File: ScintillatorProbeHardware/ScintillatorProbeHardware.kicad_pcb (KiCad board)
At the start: 2 copper layers, 99 x 80.5 mm, 14 parts

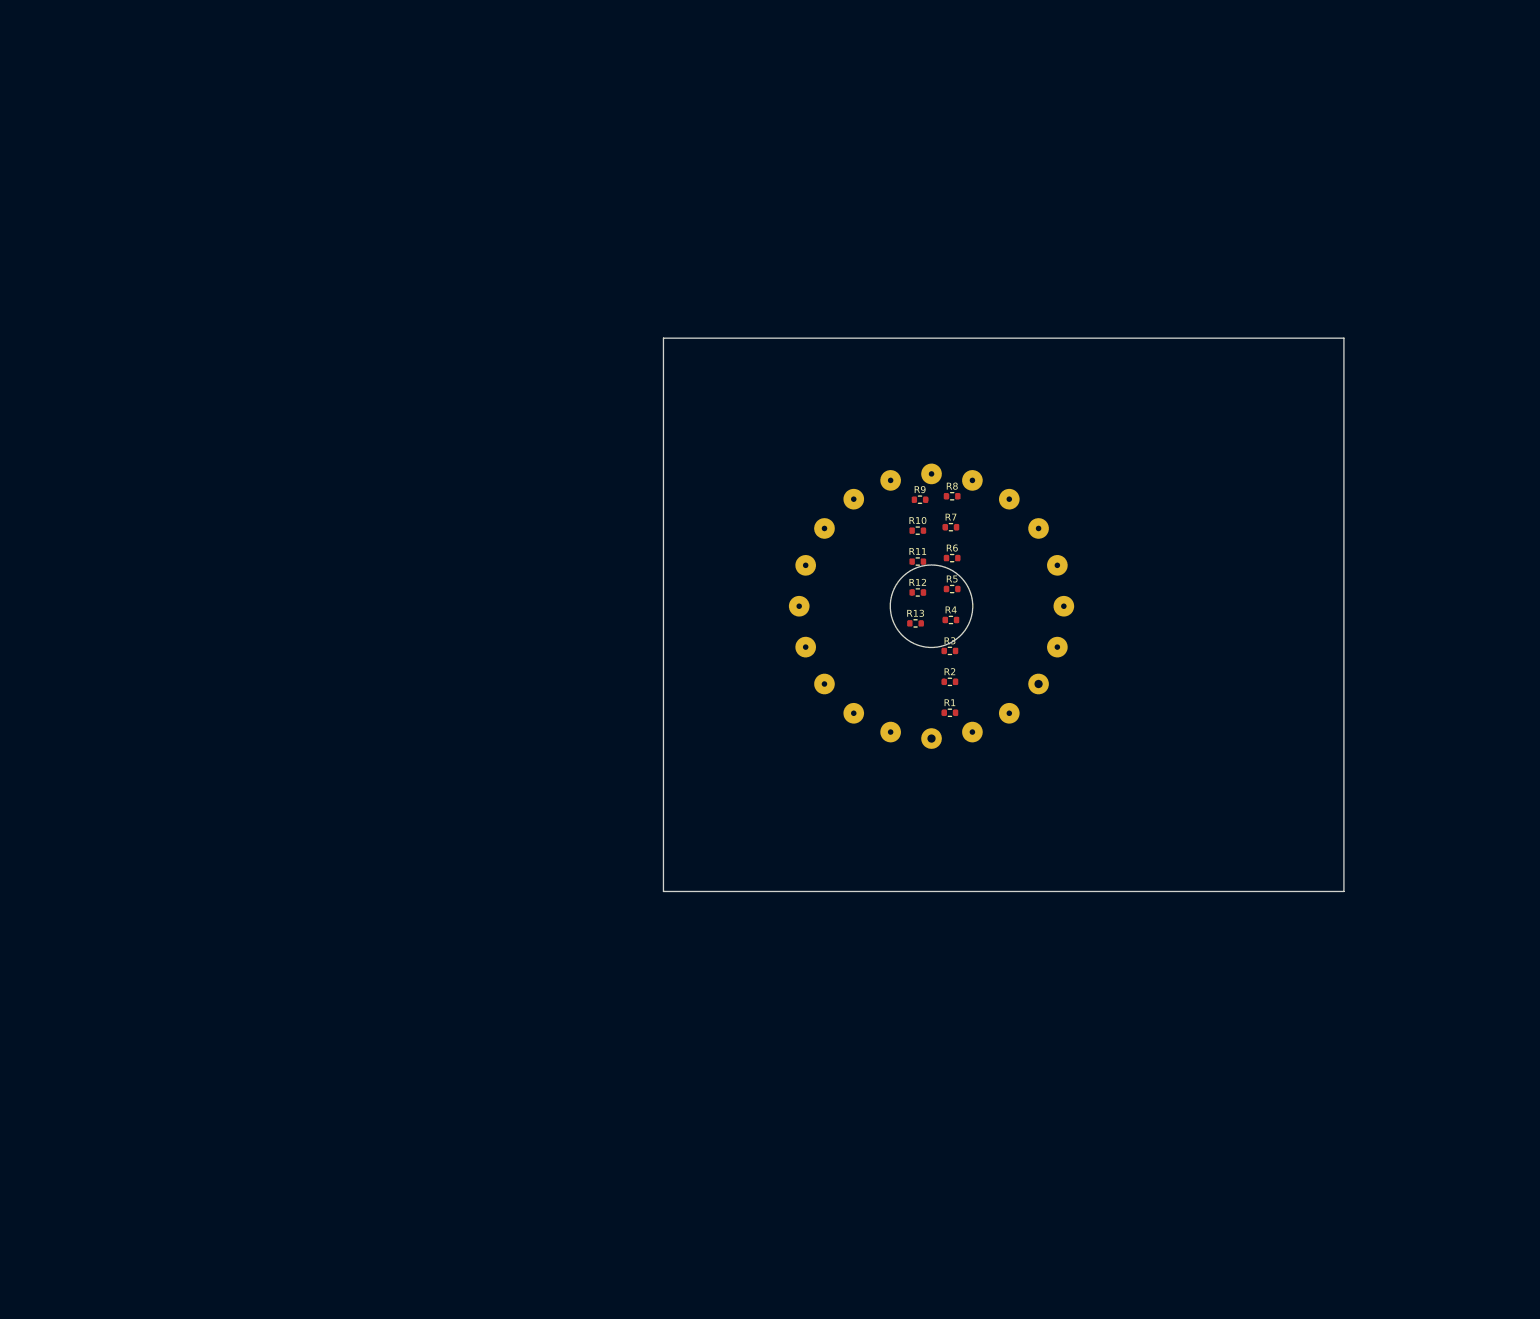
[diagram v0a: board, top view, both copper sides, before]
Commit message: PCB layout started, firmware modified for new peak detector
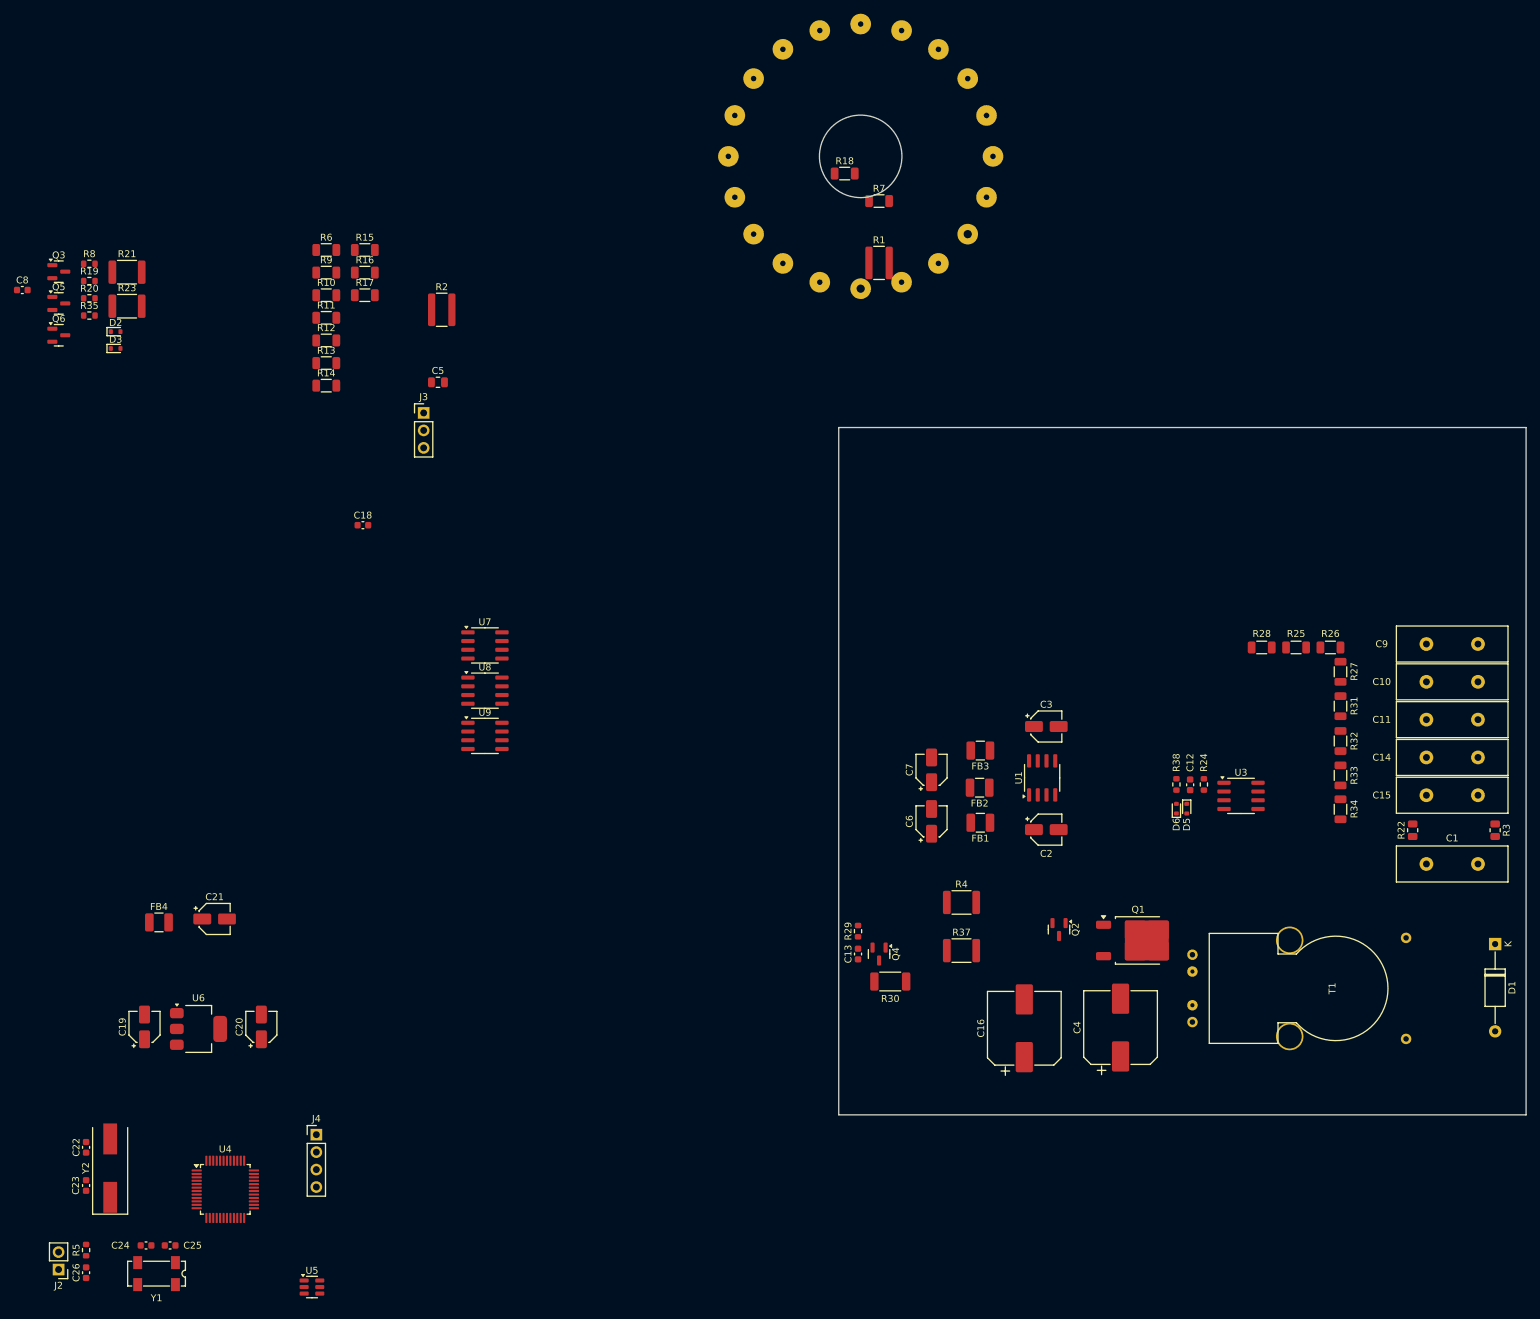
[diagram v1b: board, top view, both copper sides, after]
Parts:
- removed the R7 at (158.3, 70.5)
- added C1: 10n/3000V, Capacitor_THT:C_Disc_D16.0mm_W5.0mm_P7.50mm, F.Cu at (227.5, 119.5)
- added C10: 10n, Capacitor_THT:C_Disc_D16.0mm_W5.0mm_P7.50mm, F.Cu at (227.5, 93.0)
- added C11: 10n, Capacitor_THT:C_Disc_D16.0mm_W5.0mm_P7.50mm, F.Cu at (227.5, 98.5)
- added C12: 100n, Capacitor_SMD:C_0603_1608Metric, F.Cu at (193.1, 108.0)
- added C13: 1u, Capacitor_SMD:C_0603_1608Metric, F.Cu at (144.8, 132.6)
- added C14: 10n, Capacitor_THT:C_Disc_D16.0mm_W5.0mm_P7.50mm, F.Cu at (227.5, 104.0)
- added C15: 10n, Capacitor_THT:C_Disc_D16.0mm_W5.0mm_P7.50mm, F.Cu at (227.5, 109.5)
- added C16: 1000u, Capacitor_SMD:CP_Elec_10x10.5, F.Cu at (169.0, 143.4)
- added C18: 100n, Capacitor_SMD:C_0603_1608Metric, F.Cu at (72.8, 70.2)
- added C19: 10u, Capacitor_SMD:CP_Elec_4x5.4, F.Cu at (41.0, 143.2)
- added C2: 10u, Capacitor_SMD:CP_Elec_4x5.4, F.Cu at (172.2, 114.5)
- added C20: 10u, Capacitor_SMD:CP_Elec_4x5.4, F.Cu at (58.0, 143.2)
- added C21: 10u, Capacitor_SMD:CP_Elec_4x5.4, F.Cu at (51.2, 127.5)
- added C22: 20p, Capacitor_SMD:C_0603_1608Metric, F.Cu at (32.5, 160.7)
- added C23: 20p, Capacitor_SMD:C_0603_1608Metric, F.Cu at (32.5, 166.3)
- added C24: 20p, Capacitor_SMD:C_0603_1608Metric, F.Cu at (41.2, 175.0)
- added C25: 20p, Capacitor_SMD:C_0603_1608Metric, F.Cu at (44.7, 175.0)
- added C26: 100n, Capacitor_SMD:C_0603_1608Metric, F.Cu at (32.5, 179.0)
- added C3: 10u, Capacitor_SMD:CP_Elec_4x5.4, F.Cu at (172.2, 99.5)
- added C4: 1000u, Capacitor_SMD:CP_Elec_10x10.5, F.Cu at (183.0, 143.3)
- added C5: 10u, Capacitor_SMD:C_0805_2012Metric, F.Cu at (83.7, 49.4)
- added C6: 10u, Capacitor_SMD:CP_Elec_4x5.4, F.Cu at (155.5, 113.3)
- added C7: 10u, Capacitor_SMD:CP_Elec_4x5.4, F.Cu at (155.5, 105.8)
- added C8: 10n, Capacitor_SMD:C_0603_1608Metric, F.Cu at (23.2, 36.0)
- added C9: 10n, Capacitor_THT:C_Disc_D16.0mm_W5.0mm_P7.50mm, F.Cu at (227.5, 87.5)
- added D1: 2CL71A, Diode_THT:D_A-405_P12.70mm_Horizontal, F.Cu at (237.5, 131.2)
- added D2: D_Schottky, Diode_SMD:D_SOD-523, F.Cu at (36.8, 42.0)
- added D3: D_Schottky, Diode_SMD:D_SOD-523, F.Cu at (36.8, 44.5)
- added D5: D_Schottky, Diode_SMD:D_SOD-523, F.Cu at (192.6, 111.5)
- added D6: D_Schottky, Diode_SMD:D_SOD-523, F.Cu at (191.1, 111.5)
- added FB1: 620Ω@1MHz, Inductor_SMD:L_1210_3225Metric, F.Cu at (162.6, 113.5)
- added FB2: 620Ω@1MHz, Inductor_SMD:L_1210_3225Metric, F.Cu at (162.5, 108.4)
- added FB3: 620Ω@1MHz, Inductor_SMD:L_1210_3225Metric, F.Cu at (162.6, 103.0)
- added FB4: 620Ω@1MHz, Inductor_SMD:L_1210_3225Metric, F.Cu at (43.1, 128.0)
- added J2: Conn_01x02, Connector_PinHeader_2.54mm:PinHeader_1x02_P2.54mm_Vertical, F.Cu at (28.5, 178.5)
- added J3: Conn_01x03, Connector_PinHeader_2.54mm:PinHeader_1x03_P2.54mm_Vertical, F.Cu at (81.6, 53.9)
- added J4: Conn_01x04, Connector_PinHeader_2.54mm:PinHeader_1x04_P2.54mm_Vertical, F.Cu at (66.0, 158.9)
- added Q1: 15N10, Package_TO_SOT_SMD:TO-252-2, F.Cu at (185.6, 130.6)
- added Q2: S8050, Package_TO_SOT_SMD:SOT-23, F.Cu at (174.1, 129.0)
- added Q3: S8050, Package_TO_SOT_SMD:SOT-23, F.Cu at (28.5, 33.3)
- added Q4: AO401, Package_TO_SOT_SMD:SOT-23, F.Cu at (147.9, 132.6)
- added Q5: S8050, Package_TO_SOT_SMD:SOT-23, F.Cu at (28.5, 38.0)
- added Q6: S8050, Package_TO_SOT_SMD:SOT-23, F.Cu at (28.5, 42.6)
- added R13: 240k, Resistor_SMD:R_1206_3216Metric, F.Cu at (67.4, 46.6)
- added R14: 240k, Resistor_SMD:R_1206_3216Metric, F.Cu at (67.4, 49.9)
- added R15: 240k, Resistor_SMD:R_1206_3216Metric, F.Cu at (73.1, 30.2)
- added R16: 240k, Resistor_SMD:R_1206_3216Metric, F.Cu at (73.1, 33.5)
- added R17: 240k, Resistor_SMD:R_1206_3216Metric, F.Cu at (73.1, 36.8)
- added R19: 1k, Resistor_SMD:R_0603_1608Metric, F.Cu at (33.0, 34.7)
- added R20: 10k, Resistor_SMD:R_0603_1608Metric, F.Cu at (33.0, 37.2)
- added R21: 330R, Resistor_SMD:R_1812_4532Metric, F.Cu at (38.5, 33.4)
- added R22: 47k, Resistor_SMD:R_0805_2012Metric, F.Cu at (225.5, 114.6)
- added R23: 330R, Resistor_SMD:R_1812_4532Metric, F.Cu at (38.5, 38.4)
- added R24: 9k1, Resistor_SMD:R_0603_1608Metric, F.Cu at (195.1, 107.9)
- added R25: 1M, Resistor_SMD:R_1206_3216Metric, F.Cu at (208.5, 88.0)
- added R26: 1M, Resistor_SMD:R_1206_3216Metric, F.Cu at (213.5, 88.0)
- added R27: 1M, Resistor_SMD:R_1206_3216Metric, F.Cu at (215.0, 91.5)
- added R28: 1M, Resistor_SMD:R_1206_3216Metric, F.Cu at (203.5, 88.0)
- added R29: 100k, Resistor_SMD:R_0603_1608Metric, F.Cu at (144.8, 129.3)
- added R3: 47k, Resistor_SMD:R_0805_2012Metric, F.Cu at (237.5, 114.6)
- added R30: 47R, Resistor_SMD:R_2010_5025Metric, F.Cu at (149.5, 136.6)
- added R31: 1M, Resistor_SMD:R_1206_3216Metric, F.Cu at (215.0, 96.5)
- added R32: 1M, Resistor_SMD:R_1206_3216Metric, F.Cu at (215.0, 101.6)
- added R33: 1M, Resistor_SMD:R_1206_3216Metric, F.Cu at (215.0, 106.6)
- added R34: 1M, Resistor_SMD:R_1206_3216Metric, F.Cu at (215.0, 111.5)
- added R35: 1k, Resistor_SMD:R_0603_1608Metric, F.Cu at (33.0, 39.7)
- added R37: 330R, Resistor_SMD:R_1812_4532Metric, F.Cu at (159.9, 132.1)
- added R38: 1k, Resistor_SMD:R_0603_1608Metric, F.Cu at (191.1, 107.9)
- added T1: 24:1800, CustomParts:15kV_Transformer, F.Cu at (214.3, 137.6)
- added U1: ICL7660, Package_SO:SOIC-8_3.9x4.9mm_P1.27mm, F.Cu at (171.6, 107.0)
- added U3: LM358, Package_SO:SOIC-8_3.9x4.9mm_P1.27mm, F.Cu at (200.5, 109.6)
- added U4: STM32F103C8Tx, Package_QFP:LQFP-48_7x7mm_P0.5mm, F.Cu at (52.8, 166.8)
- added U5: USBLC6-2SC6, Package_TO_SOT_SMD:SOT-23-6, F.Cu at (65.4, 181.1)
- added U6: AMS1117-3.3, Package_TO_SOT_SMD:SOT-223-3_TabPin2, F.Cu at (48.9, 143.5)
- added U7: LM318N, Package_SO:SOIC-8_3.9x4.9mm_P1.27mm, F.Cu at (90.5, 87.7)
- added U8: LM318N, Package_SO:SOIC-8_3.9x4.9mm_P1.27mm, F.Cu at (90.5, 94.3)
- added U9: LM318N, Package_SO:SOIC-8_3.9x4.9mm_P1.27mm, F.Cu at (90.5, 100.9)
- added Y1: 32.768kHz, Crystal:Crystal_SMD_SeikoEpson_MC306-4Pin_8.0x3.2mm, F.Cu at (42.8, 179.1)
- added Y2: 8MHz, Crystal:Crystal_SMD_HC49-SD, F.Cu at (36.0, 163.8)
- R1: value 520K -> 620k; footprint Resistor_SMD:R_0603_1608Metric -> Resistor_SMD:R_1218_3246Metric
- R10, R11, R12, R6, R9: value 100K -> 240k; footprint Resistor_SMD:R_0603_1608Metric -> Resistor_SMD:R_1206_3216Metric
- R18: renamed from R13; value 100K -> 240k; footprint Resistor_SMD:R_0603_1608Metric -> Resistor_SMD:R_1206_3216Metric
- R2: value 100K -> 620k; footprint Resistor_SMD:R_0603_1608Metric -> Resistor_SMD:R_1218_3246Metric
- R4: value 100K -> 330R; footprint Resistor_SMD:R_0603_1608Metric -> Resistor_SMD:R_1812_4532Metric
- R5: value 100K -> 10k
- R7: renamed from R3; value 140K -> 336k; footprint Resistor_SMD:R_0603_1608Metric -> Resistor_SMD:R_1206_3216Metric
- R8: value 100K -> 1k
- moved R5 158.5 mm to (32.5, 175.7), turned to 90 degrees
- moved R8 130.0 mm to (33.0, 32.2)
- moved R6 101.5 mm to (67.4, 30.2)
- moved R12 93.5 mm to (67.4, 43.3)
- moved R11 93.1 mm to (67.4, 40.0)
- moved R10 92.6 mm to (67.4, 36.8)
- moved R9 92.5 mm to (67.4, 33.5)
- moved R2 91.6 mm to (84.2, 38.9)
- moved R1 66.3 mm to (147.9, 32.1)
- moved R18 66.3 mm to (142.9, 19.1)
- moved R7 66.3 mm to (147.9, 23.1)
- moved V1 66.3 mm to (145.2, 16.6)
- moved R4 41.1 mm to (159.9, 125.1)
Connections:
- net Net-(V1-Photocatode) renamed HT
- R1 pad 1: Net-(V1-D1) -> Net-(R1-Pad1)
- R10 pad 1: Net-(V1-D9) -> Net-(V1-D5)
- R10 pad 2: Net-(V1-D10) -> Net-(V1-D4)
- R11 pad 1: Net-(V1-D11) -> Net-(V1-D5)
- R11 pad 2: Net-(V1-D10) -> Net-(V1-D6)
- R12 pad 1: Net-(V1-D11) -> Net-(V1-D7)
- R12 pad 2: Net-(V1-D12) -> Net-(V1-D6)
- R18 pad 1: Net-(V1-Anode) -> GND
- R2 pad 1: Net-(V1-D1) -> Net-(R1-Pad1)
- R2 pad 2: Net-(V1-D2) -> Net-(V1-D1)
- R4 pad 1: Net-(V1-D3) -> HT_Drive_Pulse
- R4 pad 2: Net-(V1-D4) -> Net-(Q2-B)
- R5 pad 1: Net-(V1-D5) -> Net-(J2-Pin_2)
- R5 pad 2: Net-(V1-D4) -> +3.3V
- R6 pad 1: Net-(V1-D5) -> Net-(V1-D1)
- R6 pad 2: Net-(V1-D6) -> Net-(V1-D2)
- R8 pad 1: Net-(V1-D7) -> PMT_Anode
- R8 pad 2: Net-(V1-D8) -> GNDA
- R9 pad 1: Net-(V1-D9) -> Net-(V1-D3)
- R9 pad 2: Net-(V1-D8) -> Net-(V1-D4)
- V1 pad 8: Net-(V1-Anode) -> PMT_Anode
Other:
- board size 99 x 80.5 mm -> 100 x 100 mm

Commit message: PCB mostly routed
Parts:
- added C17: 1u, Capacitor_SMD:C_0603_1608Metric, F.Cu at (219.2, 64.0)
- added C27: 1u, Capacitor_SMD:C_0603_1608Metric, F.Cu at (211.2, 65.0)
- added C28: 1u, Capacitor_SMD:C_0603_1608Metric, F.Cu at (192.7, 64.0)
- added C29: 1u, Capacitor_SMD:C_0603_1608Metric, F.Cu at (164.2, 101.0)
- added C30: 1u, Capacitor_SMD:C_0603_1608Metric, F.Cu at (168.7, 93.0)
- added C31: 1u, Capacitor_SMD:C_0603_1608Metric, F.Cu at (158.2, 88.0)
- added C32: 1u, Capacitor_SMD:C_0603_1608Metric, F.Cu at (153.4, 96.7)
- added H1: MountingHole, MountingHole:MountingHole_3.2mm_M3_Pad, F.Cu at (146.0, 60.0)
- added H2: MountingHole, MountingHole:MountingHole_3.2mm_M3_Pad, F.Cu at (238.0, 60.0)
- added H3: MountingHole, MountingHole:MountingHole_3.2mm_M3_Pad, F.Cu at (238.0, 152.0)
- added H4: MountingHole, MountingHole:MountingHole_3.2mm_M3_Pad, F.Cu at (146.0, 152.0)
- added J5: ~, Connector_PinHeader_2.54mm:PinHeader_1x02_P2.54mm_Vertical, F.Cu at (-2.50, -60.5)
- added J6: ~, Connector_PinHeader_2.54mm:PinHeader_1x02_P2.54mm_Vertical, F.Cu at (235.0, 72.5)
- added J7: Conn_01x02, Connector_PinHeader_2.54mm:PinHeader_1x02_P2.54mm_Vertical, F.Cu at (172.5, 77.0)
- added Q7: S8050, Package_TO_SOT_SMD:SOT-23, F.Cu at (168.5, 81.6)
- added R36: 1k, Resistor_SMD:R_0603_1608Metric, F.Cu at (167.5, 85.0)
- added R39: 1k, Resistor_SMD:R_0603_1608Metric, F.Cu at (169.5, 77.7)
- added REF**: Symbol_HighVoltage_Triangle_6x6mm_Copper, Symbol:Symbol_HighVoltage_Triangle_6x6mm_Copper, F.Cu at (232.0, 79.5)
- added REF**: Symbol_HighVoltage_Triangle_6x6mm_Copper, Symbol:Symbol_HighVoltage_Triangle_6x6mm_Copper, F.Cu at (225.5, 150.5)
- added REF**: Symbol_HighVoltage_Triangle_6x6mm_Copper, Symbol:Symbol_HighVoltage_Triangle_6x6mm_Copper, F.Cu at (217.0, 122.0)
- added REF**: Symbol_HighVoltage_Triangle_6x6mm_Copper, Symbol:Symbol_HighVoltage_Triangle_6x6mm_Copper, B.Cu at (217.5, 141.0)
- added REF**: Symbol_HighVoltage_Triangle_6x6mm_Copper, Symbol:Symbol_HighVoltage_Triangle_6x6mm_Copper, B.Cu at (215.8, 100.0)
- added REF**: Symbol_HighVoltage_Triangle_6x6mm_Copper, Symbol:Symbol_HighVoltage_Triangle_6x6mm_Copper, B.Cu at (236.0, 80.5)
- added REF**: Symbol_HighVoltage_Triangle_6x6mm_Copper, Symbol:Symbol_HighVoltage_Triangle_6x6mm_Copper, B.Cu at (233.0, 114.5)
- moved R8 197.0 mm to (226.5, 69.2), turned to -90 degrees
- moved R18 195.2 mm to (-36.5, -58.0)
- moved R7 191.9 mm to (-27.5, -55.0)
- moved R20 186.7 mm to (215.7, 75.5), turned to 180 degrees
- moved R19 184.2 mm to (214.7, 65.0), turned to 180 degrees
- moved R1 184.1 mm to (-11.0, -61.0)
- moved Q3 181.5 mm to (206.6, 68.6), turned to 90 degrees
- moved C8 180.7 mm to (201.0, 68.2), turned to 90 degrees
- moved Q6 180.2 mm to (206.0, 73.6), turned to -90 degrees
- moved C26 178.1 mm to (183.5, 84.5)
- moved R5 178.1 mm to (183.5, 81.2)
- moved J2 178.1 mm to (179.5, 84.0)
- moved Q5 175.6 mm to (200.5, 73.6), turned to -90 degrees
- moved R23 170.7 mm to (204.0, 79.9), turned to -90 degrees
- moved R21 167.6 mm to (199.5, 79.9), turned to 90 degrees
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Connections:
- D6 pad 1: +3.3V -> +3.3VA
- R1 pad 2: HT -> Net-(J5-Pin_1)
- R18 pad 1: GND -> Net-(J5-Pin_2)
- U4 pad 10: unconnected-(U4-PA0-Pad10) -> HT_Sense
- U4 pad 11: unconnected-(U4-PA1-Pad11) -> Peak_Sense
- U4 pad 13: unconnected-(U4-PA3-Pad13) -> Buzzer
- U4 pad 16: unconnected-(U4-PA6-Pad16) -> Peak_Reset
- U4 pad 29: unconnected-(U4-PA8-Pad29) -> HT_Drive_Pulse
- U5 pad 5: +5V -> +3.3V
- V1 pad 20: HT -> Net-(J5-Pin_1)
- V1 pad 8: PMT_Anode -> Net-(J5-Pin_2)
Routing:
- net +5VA: track 0.00 -> 145.3 mm, vias 0 -> 9
- net +3.3V: track 0.00 -> 124.1 mm, vias 0 -> 7
- net -5VA: track 0.00 -> 96.8 mm, vias 0 -> 4
- net +5V: track 0.00 -> 84.5 mm, vias 0 -> 3
- net +3.3VA: track 0.00 -> 74.6 mm, vias 0 -> 5
- net HT: track 0.00 -> 55.9 mm
- net Peak_Reset: track 0.00 -> 46.5 mm, vias 0 -> 2
- net GNDA: track 0.00 -> 45.7 mm, vias 0 -> 209
- net HT_Drive_Pulse: track 0.00 -> 39.6 mm, vias 0 -> 2
- net HT_Sense: track 0.00 -> 36.8 mm, vias 0 -> 2
- net Peak_Sense: track 0.00 -> 33.7 mm
- net Net-(U4-PD0): track 0.00 -> 31.5 mm, vias 0 -> 2
- net Net-(U4-PC14): track 0.00 -> 30.9 mm
- net Net-(J2-Pin_2): track 0.00 -> 28.3 mm
- net Net-(U4-PD1): track 0.00 -> 28.2 mm, vias 0 -> 2
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- added copper zone on B.Cu, net GND
- added copper zone on F.Cu, net GND
- added copper zone on B.Cu, net GNDA
- added copper zone on F.Cu, net GNDA
- added copper zone on F.Cu, net Net-(Q1-D)
- added copper zone on F.Cu, net Net-(Q4-D)
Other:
- board text added: "Designed by Michal Tomek"
- board text added: "Scintillator Detector Counter"
